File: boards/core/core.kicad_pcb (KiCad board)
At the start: 2 copper layers, 215 x 100 mm, 371 parts, among them J201 Conn_02x08_Counter_Clockwise, J202 Conn_02x08_Counter_Clockwise, J203 Conn_02x08_Counter_Clockwise, J204 Conn_02x08_Counter_Clockwise, J205 Conn_01x03, J206 Conn_01x03, J207 Screw_Terminal_01x03, J208 Conn_01x03, J209 Conn_01x03, J214 Conn_02x04_Counter_Clockwise, Q201 2N3906, Q202 BC847BS, Q203 MMBFJ111, Q204 2N3906, Q205 BC847BS, Q206 MMBFJ111, Q207 BC847BS, Q208 BC548C, Q209 BC548C, Q210 BC548C, Q212 MMBT5551, Q213 MMBT5551, Q214 MMBT5551, U201 TL072, U202 TL072, U203 LM311, U204 TL072, U205 TL072, U206 LM311, U207 TL072, U208 TL072, U209 TL072, U210 TL072, U211 TL072, U212 4002, U213 LM358, U214 TL072, U215 CD4053B, U216 NE5532, U217 TL072, U218 TL072, U219 TL072, U220 TL072, U221 TL072, U222 TL072, U223 TL072, U224 LM336M-5.0/TR, U225 TL072, U226 TL072, U227 TL072, U228 CD4040BM96

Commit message: Removed VCA rejection trimpot
https://github.com/shmoergh/hog/issues/8

Also updated Core board footprints to work with fcking KiCad 8
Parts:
- removed RV_VCA_REJECTION201: 10k, Potentiometer_THT:Potentiometer_Bourns_3006P_Horizontal
- Q203, Q206: footprint PCM_Package_TO_SOT_SMD_AKL:SOT-23_Handsoldering -> Package_TO_SOT_SMD:SOT-23_Handsoldering
- moved TP226 0.63 mm to (183.2, 182.4)
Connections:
- R235 pad 2: Net-(R235-Pad2) -> +12V
- R237 pad 2: Net-(R237-Pad2) -> +12V
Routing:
- net Net-(R235-Pad2): track 47.9 -> 0.00 mm, vias 2 -> 0
- net Net-(R237-Pad2): track 32.9 -> 0.00 mm
- net Net-(C284-Pad2): track 66.2 -> 47.5 mm
- net +12V: track 1194.4 -> 1195.3 mm
- net GND: vias 388 -> 407

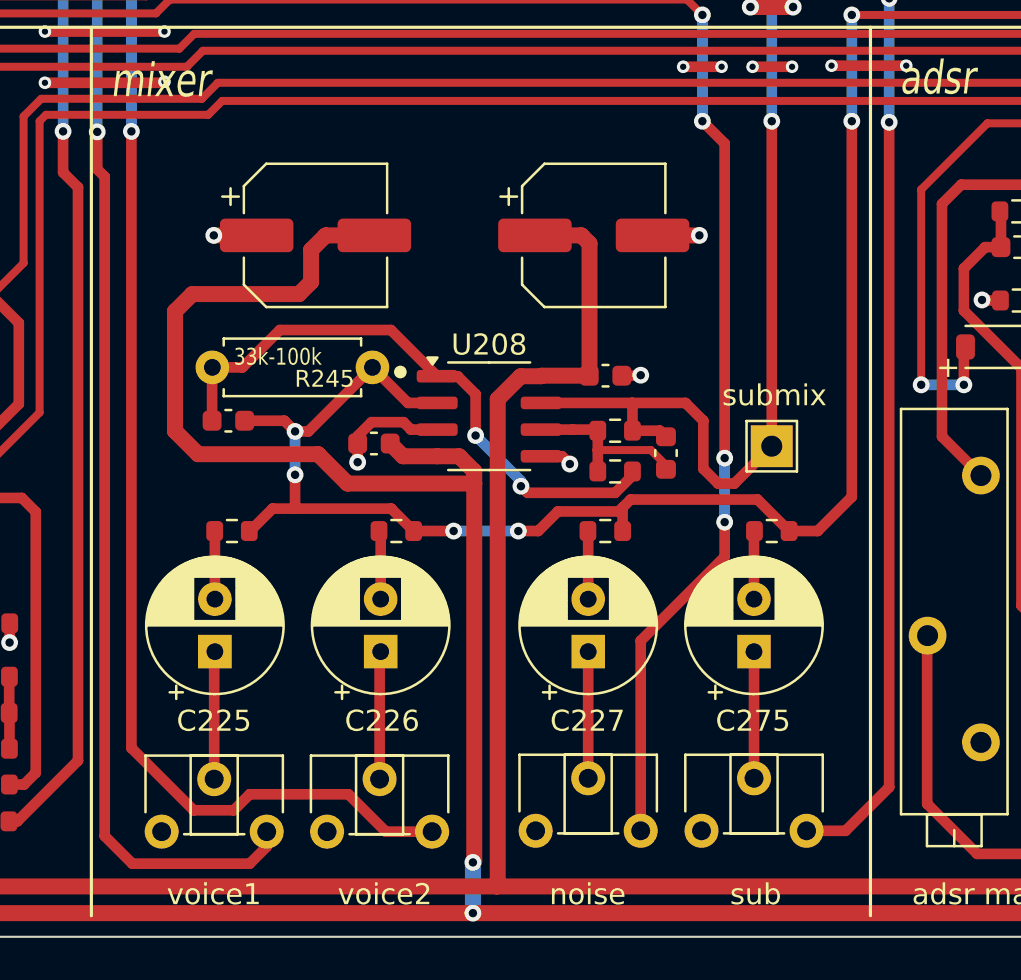
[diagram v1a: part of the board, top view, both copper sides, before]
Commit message: Replaced mixer input caps to SMD
https://github.com/shmoergh/hog/issues/26
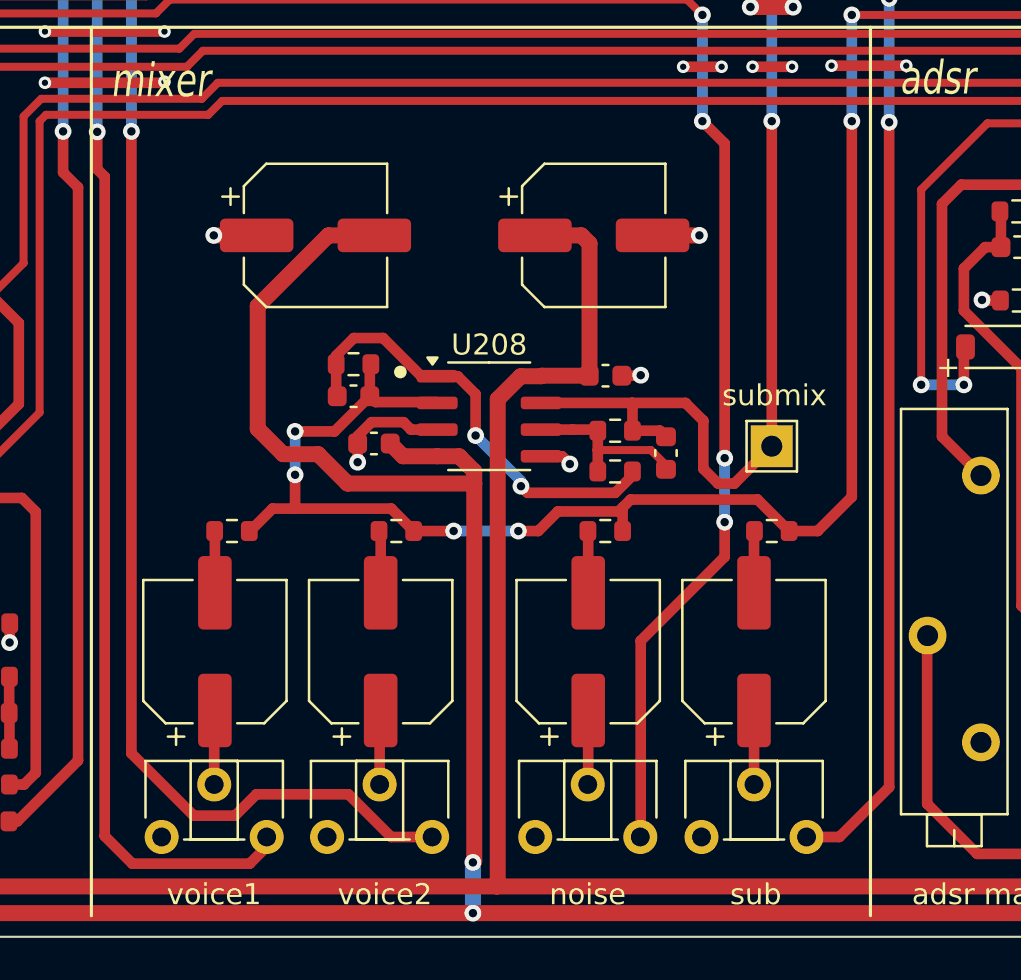
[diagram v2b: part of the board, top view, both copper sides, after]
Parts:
- C225, C226, C227, C275: footprint Capacitor_THT:CP_Radial_D6.3mm_P2.50mm -> Capacitor_SMD:CP_Elec_6.3x5.4
- R245: value 33k-100k -> 33k; footprint Shmoergh_Custom_Footprints:R_Axial_DIN0207_L6.3mm_D2.5mm_P7.62mm_Horizontal -> Resistor_SMD:R_0603_1608Metric
- moved C282 6.07 mm to (165.8, 237.3)
- moved R245 0.91 mm to (165.8, 235.7)
- moved RV202 0.29 mm to (174.4, 258.2)
- moved RV204 0.29 mm to (182.3, 258.2)
- moved RV201 0.25 mm to (156.6, 258.2)
- moved RV205 0.25 mm to (164.5, 258.2)
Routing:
- net -12V: track 1097.2 -> 1088.5 mm
- net Net-(C282-Pad2): track 28.3 -> 21.3 mm
- net Net-(C226-Pad1): track 6.09 -> 3.54 mm
- net Net-(C275-Pad1): track 6.04 -> 3.52 mm
- net Net-(C227-Pad1): track 6.04 -> 3.53 mm
- net Net-(C225-Pad1): track 6.13 -> 3.84 mm
- net EXTERNAL_INPUT: track 128.7 -> 126.5 mm

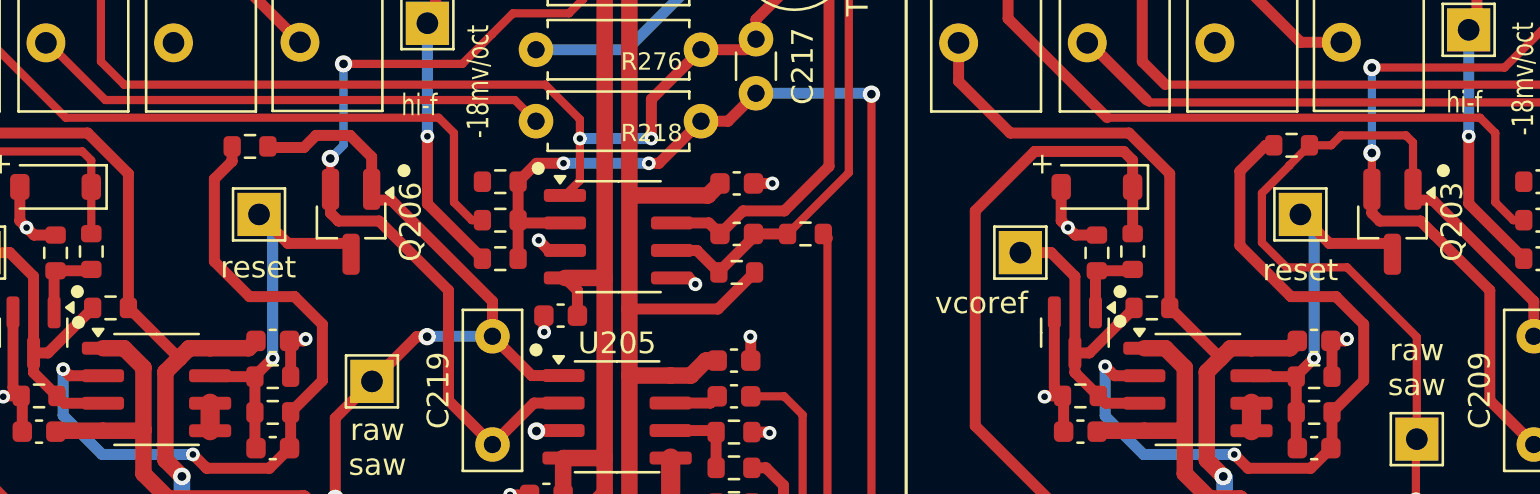
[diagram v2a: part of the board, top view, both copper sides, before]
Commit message: Added THT footprint to J111 in VCOs
https://github.com/shmoergh/hog/issues/10
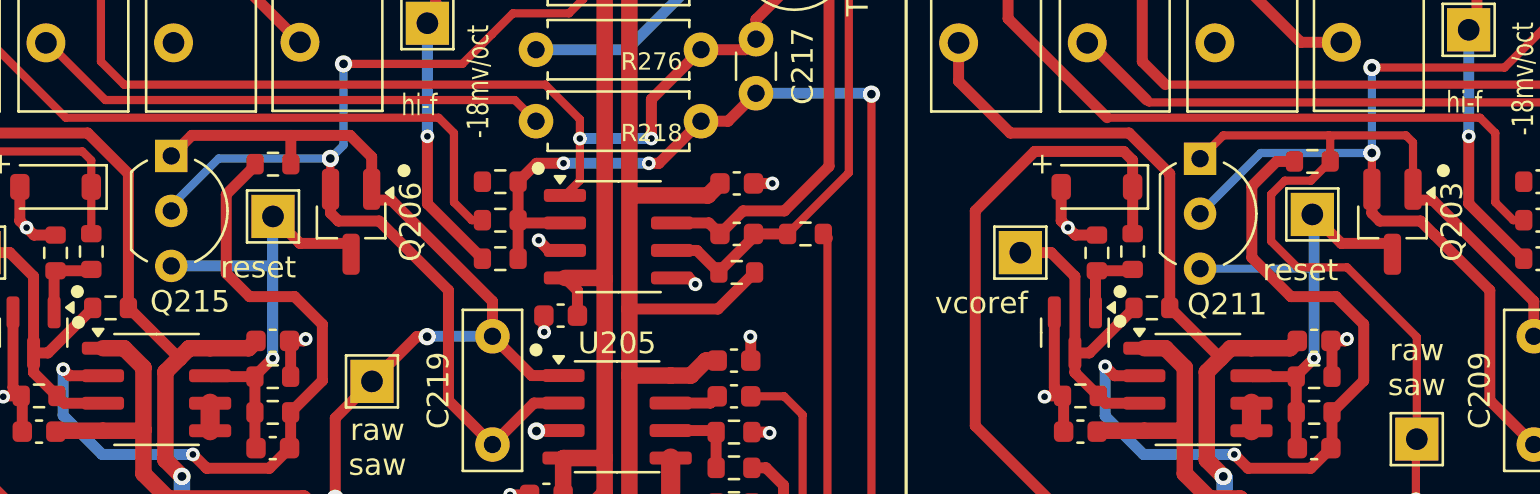
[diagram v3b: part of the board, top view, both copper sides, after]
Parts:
- added Q211: J111, Package_TO_SOT_THT:TO-92_Inline_Wide, F.Cu at (123.6, 188.3)
- added Q215: J111, Package_TO_SOT_THT:TO-92_Inline_Wide, F.Cu at (76.1, 188.1)
- moved R226 1.34 mm to (80.8, 188.5)
- moved R211 1.21 mm to (128.8, 188.4)
- moved TP208 0.65 mm to (80.8, 190.9)
- moved TP204 0.55 mm to (128.8, 190.8)
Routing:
- net Net-(Q202-C2): track 48.8 -> 57.9 mm
- net Net-(Q205-C2): track 49.0 -> 57.5 mm
- net /VCO 2/RAW_SAW: track 203.8 -> 210.0 mm
- net /VCO/RAW_SAW: track 185.0 -> 190.9 mm
- net Net-(Q203-G): track 18.3 -> 22.8 mm
- net Net-(Q206-G): track 18.3 -> 22.0 mm
- net Net-(U206-+): track 34.2 -> 33.3 mm
- net Net-(U203-+): track 35.2 -> 34.6 mm
